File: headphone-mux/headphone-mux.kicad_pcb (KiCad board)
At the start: 4 copper layers, 543 parts, among them J5 Mixer Audio In, U100 OPA1604, U101 OPA1604, U102 OPA1604, U103 OPA1602, U104 OPA1604, U105 OPA1604, U106 OPA1604, U107 OPA1604, U108 OPA1602, U109 OPA1604, U11 ADG734, U110 OPA1604, U111 OPA1604, U112 OPA1604, U113 OPA1602, U114 OPA1604, U115 OPA1604, U116 OPA1604, U117 OPA1604, U118 OPA1602, U119 OPA1604, U120 OPA1604, U121 OPA1604, U13 ADG734, U14 ADG734, U16 ADG734, U4 ADG715, U57 ADG708, U58 ADG708, U59 ADG708, U60 ADG708, U61 ADG708, U62 ADG708, U63 ADG708, U64 ADG708, U65 ADG708, U66 ADG708, U67 ADG708, U68 ADG708, U69 ADG708, U70 ADG708, U71 ADG708, U72 ADG708, U73 TCA9555, U74 TCA9555, U75 TCA9555, U76 TCA9555, U77 OPA1604, U78 OPA1602, U79 OPA1604, U80 OPA1604, U81 OPA1604, U82 OPA1604, U83 OPA1602, U84 OPA1604, U85 OPA1604, U86 OPA1604, U87 OPA1604, U88 OPA1602, U89 OPA1604, U9 ADG715, U90 OPA1604, U91 OPA1604, U92 OPA1604, U93 OPA1602, U94 OPA1604, U95 OPA1604, U96 OPA1604, U97 OPA1604, U98 OPA1602, U99 OPA1604

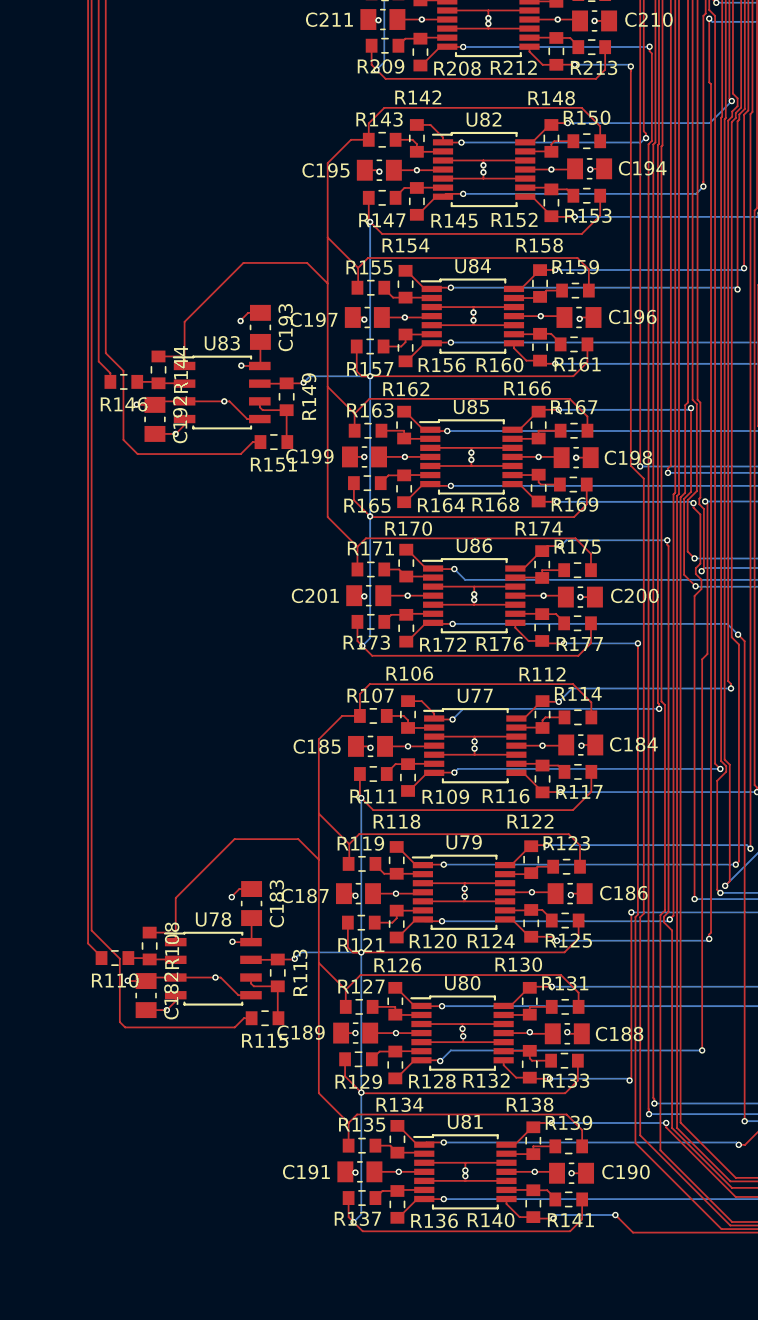
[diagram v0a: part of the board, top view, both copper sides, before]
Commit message: Second 1:8 DA layout re annotated
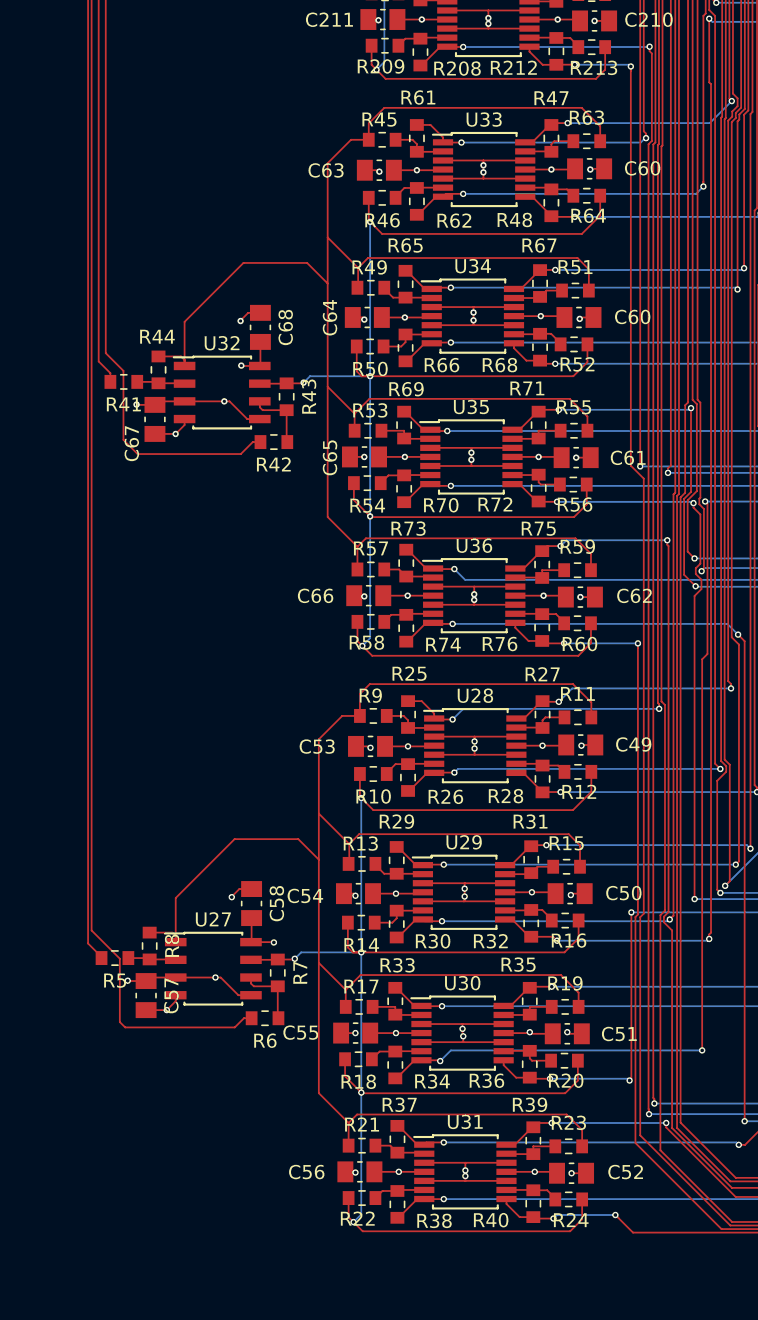
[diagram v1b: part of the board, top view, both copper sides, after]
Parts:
- renumbered C184 to C49, C186 to C50, C188 to C51, C190 to C52, C185 to C53, C187 to C54, C189 to C55, C191 to C56, C182 to C57, C183 to C58, C194 to C60, C196 to C60, C198 to C61, C200 to C62, C195 to C63, C197 to C64, C199 to C65, C201 to C66, C192 to C67, C193 to C68, R111 to R10, R114 to R11, R117 to R12, R119 to R13, R121 to R14, R123 to R15, R125 to R16, R127 to R17, R129 to R18, R131 to R19, R133 to R20, R135 to R21, R137 to R22, R139 to R23, R141 to R24, R106 to R25, R109 to R26, R112 to R27, R116 to R28, R118 to R29, R120 to R30, R122 to R31, R124 to R32, R126 to R33, R128 to R34, R130 to R35, R132 to R36, R134 to R37, R136 to R38, R138 to R39, R140 to R40, R146 to R41, R151 to R42, R149 to R43, R144 to R44, R143 to R45, R147 to R46, R148 to R47, R152 to R48, R155 to R49, R110 to R5, R157 to R50, R159 to R51, R161 to R52, R163 to R53, R165 to R54, R167 to R55, R169 to R56, R171 to R57, R173 to R58, R175 to R59, R115 to R6, R177 to R60, R142 to R61, R145 to R62, R150 to R63, R153 to R64, R154 to R65, R156 to R66, R158 to R67, R160 to R68, R162 to R69, R113 to R7, R164 to R70, R166 to R71, R168 to R72, R170 to R73, R172 to R74, R174 to R75, R176 to R76, R108 to R8, R107 to R9, U78 to U27, U77 to U28, U79 to U29, U80 to U30, U81 to U31, U83 to U32, U82 to U33, U84 to U34, U85 to U35, U86 to U36

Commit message: dev 2 1:8 DA re annotated
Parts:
- renumbered C204 to C69, C206 to C70, C208 to C71, C210 to C72, C205 to C73, C207 to C74, C209 to C75, C211 to C76, C202 to C77, C203 to C78, R188 to R100, R190 to R101, R192 to R102, R194 to R103, R196 to R104, R198 to R105, R200 to R106, R202 to R107, R204 to R108, R206 to R109, R208 to R110, R210 to R111, R212 to R112, R182 to R77, R187 to R78, R185 to R79, R180 to R80, R179 to R81, R183 to R82, R186 to R83, R189 to R84, R191 to R85, R193 to R86, R195 to R87, R197 to R88, R199 to R89, R201 to R90, R203 to R91, R205 to R92, R207 to R93, R209 to R94, R211 to R95, R213 to R96, R178 to R97, R181 to R98, R184 to R99, U88 to U37, U87 to U38, U89 to U39, U90 to U40, U91 to U41
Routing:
- net /Audio Mux and Control/Headset LR audio out Mux and Source Selection/Dev 2 1:8 DA/R_Distro_Bus: track 121.9 -> 122.9 mm, vias 4 -> 5

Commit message: Dev 3 1:8 DA re annotated
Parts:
- renumbered C214 to C79, C216 to C80, C218 to C81, C220 to C82, C215 to C83, C217 to C84, C219 to C85, C221 to C86, C212 to C87, C213 to C88, R218 to R113, R223 to R114, R221 to R115, R216 to R116, R215 to R117, R219 to R118, R222 to R119, R225 to R120, R227 to R121, R229 to R122, R231 to R123, R233 to R124, R235 to R125, R237 to R126, R239 to R127, R241 to R128, R243 to R129, R245 to R130, R247 to R131, R249 to R132, R214 to R133, R217 to R134, R220 to R135, R224 to R136, R226 to R137, R228 to R138, R230 to R139, R232 to R140, R234 to R141, R236 to R142, R238 to R143, R240 to R144, R242 to R145, R244 to R146, R246 to R147, R248 to R148, U93 to U42, U92 to U43, U94 to U44, U95 to U45, U96 to U46
